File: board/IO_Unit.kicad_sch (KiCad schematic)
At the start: 2 parts, among them U3 MCP23017_SS, U5 TCA9548APWR

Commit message: [6-5-2024] Create I/O
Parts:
- removed U5: TCA9548APWR, Package_SO:TSSOP-24_4.4x7.8mm_P0.65mm, symbol Interface_Expansion:TCA9548APWR
- added JP1: MCP23017_ADDR_A2, Jumper:SolderJumper-3_P1.3mm_Open_Pad1.0x1.5mm_NumberLabels, symbol Jumper:SolderJumper_3_Open
- added JP2: MCP23017_ADDR_A1, Jumper:SolderJumper-3_P1.3mm_Open_Pad1.0x1.5mm_NumberLabels, symbol Jumper:SolderJumper_3_Open
- added JP3: MCP23017_ADDR_A0, Jumper:SolderJumper-3_P1.3mm_Open_Pad1.0x1.5mm_NumberLabels, symbol Jumper:SolderJumper_3_Open
- added R16, R17: 1k, Resistor_SMD:R_0805_2012Metric_Pad1.20x1.40mm_HandSolder, symbol Device:R_US
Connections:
- net GND: now reaches U3.10 (VSS)
- net GND: now also JP1.1 (A), JP2.1 (A), JP3.1 (A)
- net SCK_MCP23017: now reaches U3.12 (SCK)
- net SCK_MCP23017: now also R16.2
- net SDA_MCP23017: now reaches U3.13 (SDA)
- net SDA_MCP23017: now also R17.2
- net at U3.15 (A0): now also JP3.2 (C)
- net at U3.16 (A1): now also JP2.2 (C)
- net at U3.17 (A2): now also JP1.2 (C)
- net +5V: now reaches U3.18 (~{RESET})
- net +5V: now also U3.9 (VDD), JP1.3 (B), JP2.3 (B), JP3.3 (B), R16.1, R17.1
- net INTB_MCP23017: now reaches U3.19 (INTB)
- net INTA_MCP23017: now reaches U3.20 (INTA)
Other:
- moved on the sheet: U3

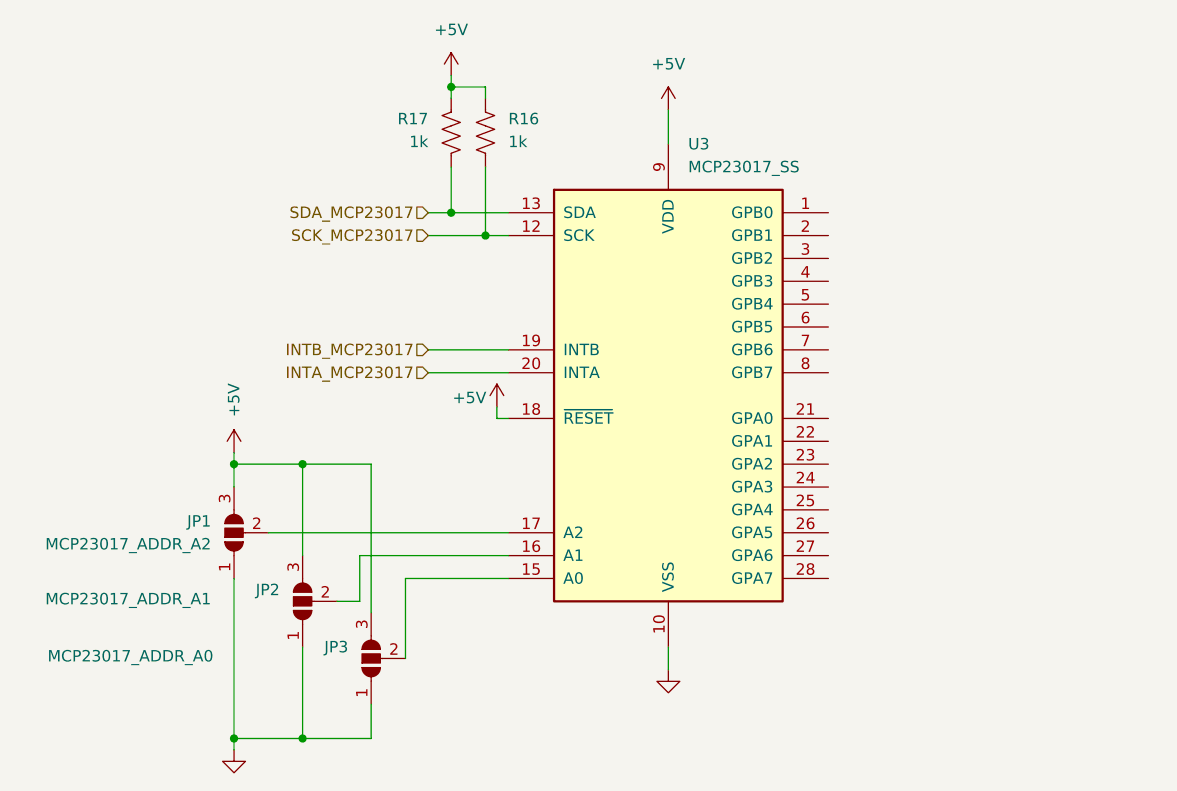
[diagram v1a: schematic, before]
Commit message: [23-5-2024] add micro sd card connector and MAX31856 Thermocouple driver
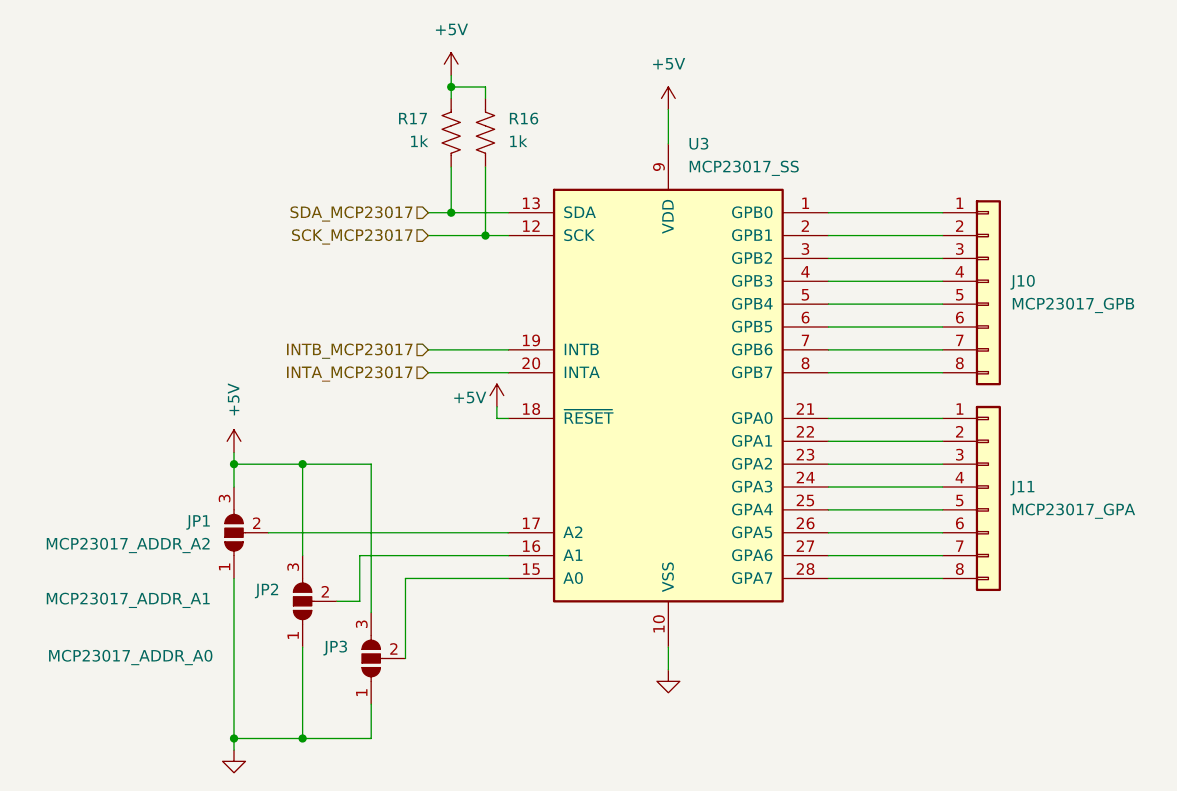
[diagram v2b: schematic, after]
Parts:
- added J10: MCP23017_GPB, Connector_Molex:Molex_KK-254_AE-6410-08A_1x08_P2.54mm_Vertical, symbol Connector_Generic:Conn_01x08
- added J11: MCP23017_GPA, Connector_Molex:Molex_KK-254_AE-6410-08A_1x08_P2.54mm_Vertical, symbol Connector_Generic:Conn_01x08
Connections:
- net at U3.1 (GPB0): now also J10.1 (Pin_1)
- net at U3.2 (GPB1): now also J10.2 (Pin_2)
- net at U3.21 (GPA0): now also J11.1 (Pin_1)
- net at U3.22 (GPA1): now also J11.2 (Pin_2)
- net at U3.23 (GPA2): now also J11.3 (Pin_3)
- net at U3.24 (GPA3): now also J11.4 (Pin_4)
- net at U3.25 (GPA4): now also J11.5 (Pin_5)
- net at U3.26 (GPA5): now also J11.6 (Pin_6)
- net at U3.27 (GPA6): now also J11.7 (Pin_7)
- net at U3.28 (GPA7): now also J11.8 (Pin_8)
- net at U3.3 (GPB2): now also J10.3 (Pin_3)
- net at U3.4 (GPB3): now also J10.4 (Pin_4)
- net at U3.5 (GPB4): now also J10.5 (Pin_5)
- net at U3.6 (GPB5): now also J10.6 (Pin_6)
- net at U3.7 (GPB6): now also J10.7 (Pin_7)
- net at U3.8 (GPB7): now also J10.8 (Pin_8)
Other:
- company: (none) -> AHAH_TERROR
- title: (none) -> IO Expansion
